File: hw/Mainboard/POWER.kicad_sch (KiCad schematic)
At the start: 67 parts, among them J10 5V PWR, J11 9V POWER, J18 PET POWER, J20 5V PWR, J7 9V POWER, U10 LM317AG-TN3-R, U13 AMS1117-3.3, U15 LM317AG-TN3-R, U17 LM317AG-TN3-R

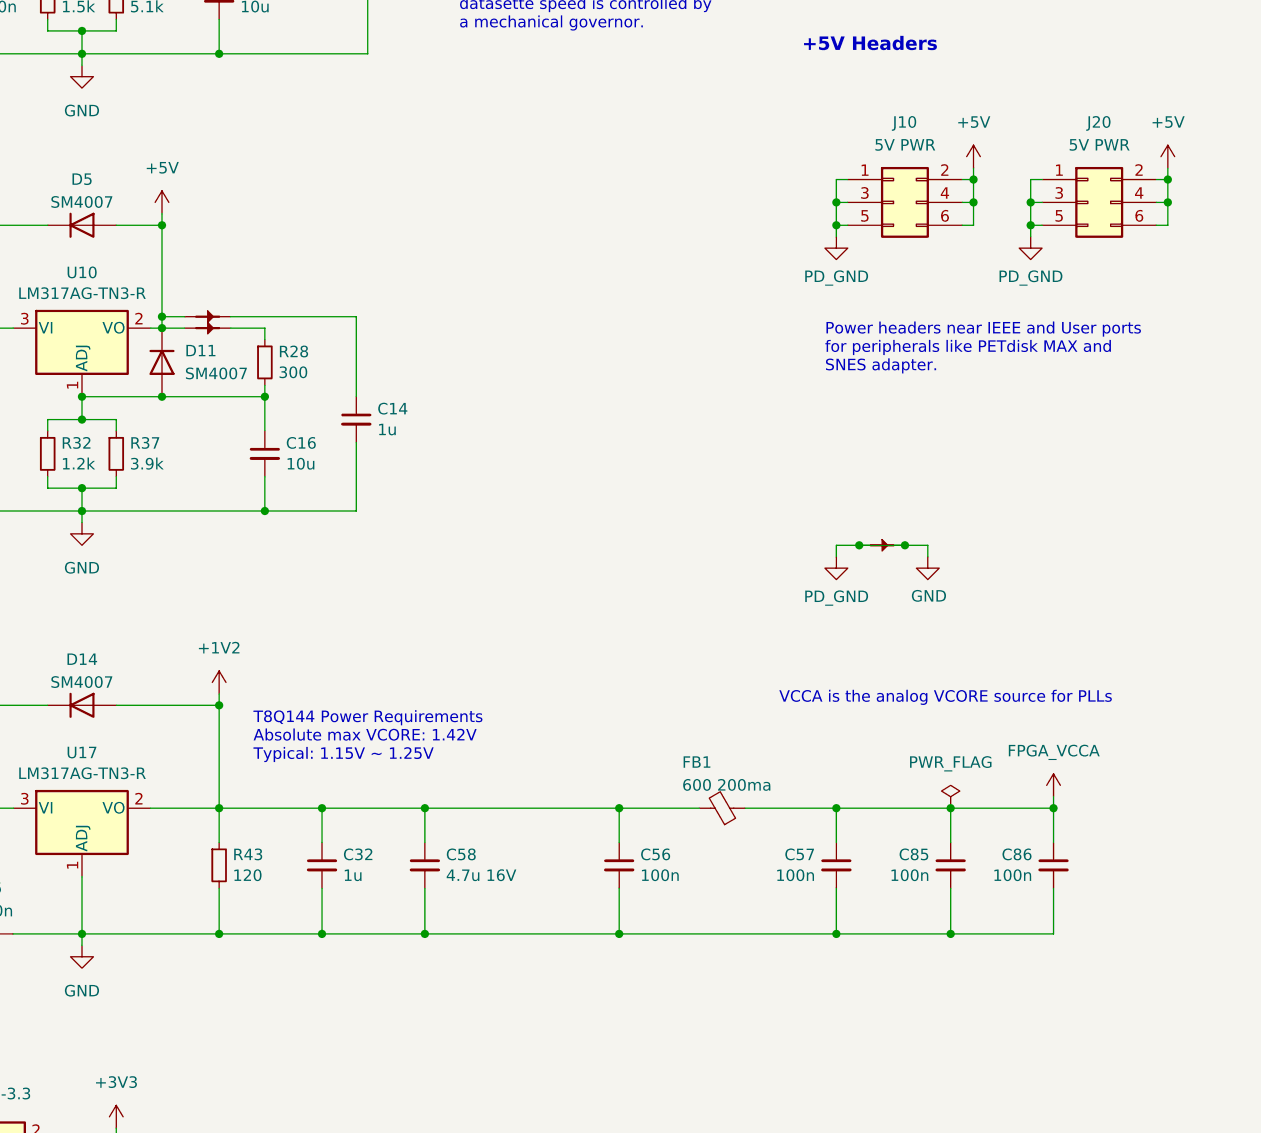
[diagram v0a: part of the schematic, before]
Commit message: hw: heat sink, trace size, more stitching
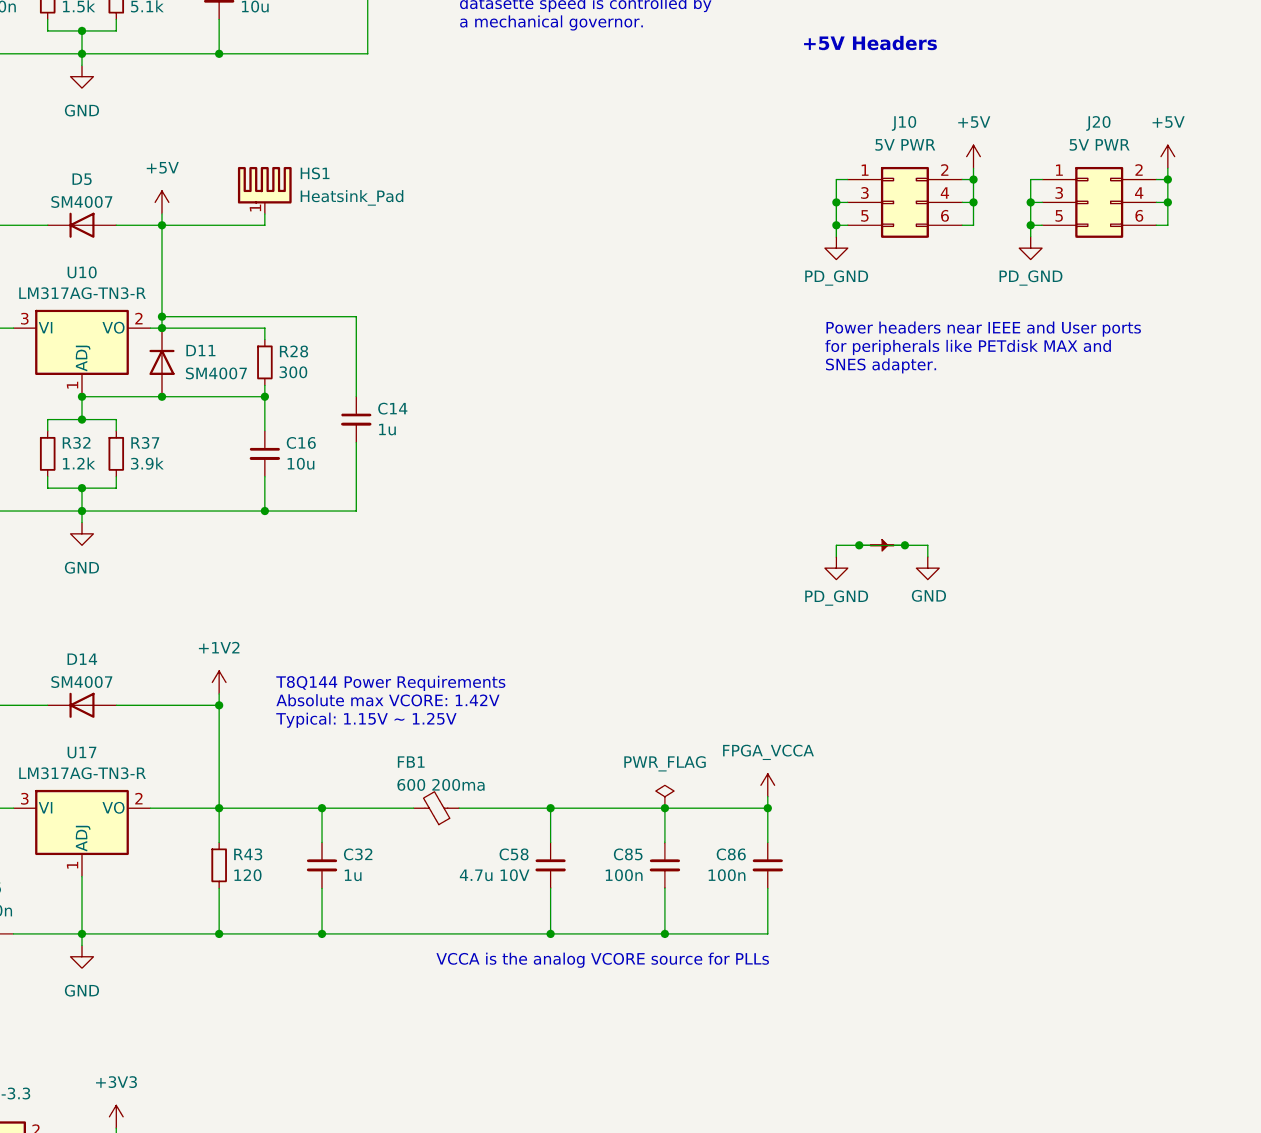
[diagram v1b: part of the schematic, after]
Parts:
- removed C56, C57: 100n, Capacitor_SMD:C_0402_1005Metric, symbol Device:C_Small
- removed PT3, PT34: PowerTie_2, PET:NetTie-2_SMD_Pad_1.6_to_0.4mm, symbol PET:PowerTie_2
- added HS1: Heatsink_Pad, PET:V1100SMDBL, symbol Mechanical:Heatsink_Pad
- C58: value 4.7u 16V -> 4.7u 10V; footprint Capacitor_SMD:C_0603_1608Metric -> Capacitor_SMD:C_0402_1005Metric; LCSC C19666 -> C23733
- U10, U15: footprint PET:TO-252-2_ThermalVias -> Package_TO_SOT_SMD:TO-252-2
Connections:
- net +1V2: no longer C58.1
- net +5V: now also C14.1, R28.1, HS1.1
- net FPGA_VCCA: now also C58.1
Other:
- moved on the sheet: C58, C85, C86, FB1

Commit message: HW: Rename 'MFR' to 'MPN' in BOM
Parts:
- HS1: MFR V-1100-SMD/B-L -> (none); MPN (none) -> V-1100-SMD/B-L
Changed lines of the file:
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@@
       (effects (font (size 1.27 1.27)) hide)
     )
-    (property "MFR" "V-1100-SMD/B-L" (id 5) (at 151.13 72.39 0)
+    (property "MPN" "V-1100-SMD/B-L" (id 6) (at 151.13 72.39 0)
       (effects (font (size 1.27 1.27)) hide)
     )

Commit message: hw: add more Mouse part numbers
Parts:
- J10, J20: MOUSER (none) -> 649-1012938195002BLF
- J11: MOUSER (none) -> 649-1012937893602BLF
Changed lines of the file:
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@@
+      (effects (font (size 1.27 1.27)) hide)
+    )
+    (property "MOUSER" "649-1012937893602BLF" (id 4) (at 87.63 41.91 0)
       (effects (font (size 1.27 1.27)) hide)
     )
@@
     )
     (property "Datasheet" "" (id 3) (at 242.57 73.66 0)
+      (effects (font (size 1.27 1.27)) hide)
+    )
+    (property "MOUSER" "649-1012938195002BLF" (id 4) (at 242.57 73.66 0)
       (effects (font (size 1.27 1.27)) hide)
     )
@@
       (effects (font (size 1.27 1.27)) hide)
     )
-    (property "Datasheet" "~" (id 3) (at 151.4348 73.66 0)
+    (property "Datasheet" "http://www.assmann-wsw.com/uploads/datasheets/ASS_0855_HS.pdf" (id 3) (at 151.4348 73.66 0)
       (effects (font (size 1.27 1.27)) hide)
     )
@@
       (effects (font (size 1.27 1.27)) hide)
     )
+    (property "MOUSER" "649-1012938195002BLF" (id 4) (at 220.98 73.66 0)
+      (effects (font (size 1.27 1.27)) hide)
+    )

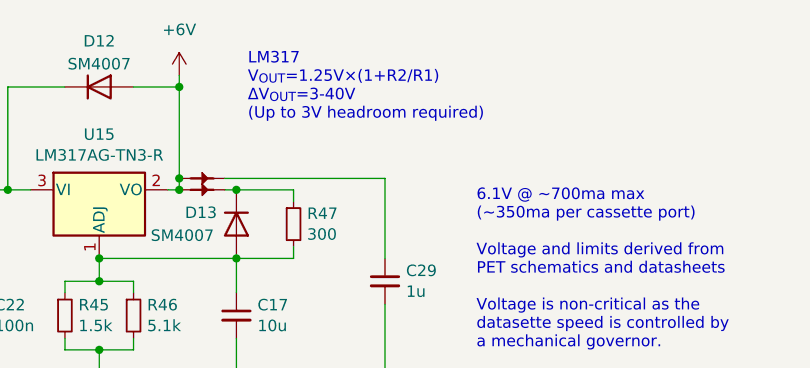
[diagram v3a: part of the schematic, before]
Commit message: hw: PN for IC, remove dup PNs, remove redundant headroom text on PWR
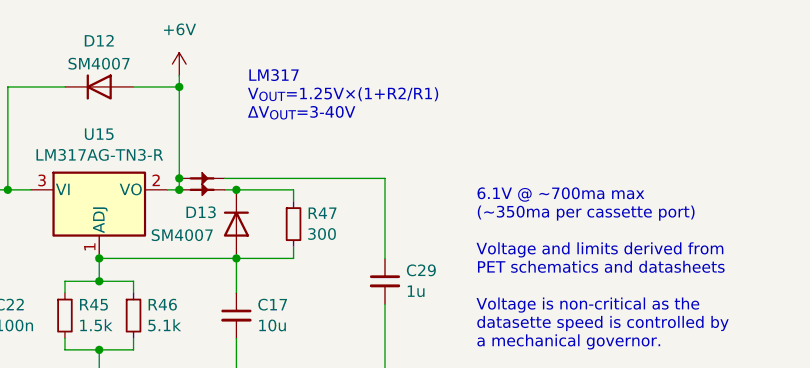
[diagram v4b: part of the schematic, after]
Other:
- note added: "LM317 V_{OUT}=1.25V×(1+R2/R1) ΔV_{OUT}=3-40V"
- note removed: "LM317 V_{OUT}=1.25V×(1+R2/R1) ΔV_{OUT}=3-40V (Up to 3V headroom required)"
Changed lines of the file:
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@@
     (effects (font (size 1.27 1.27)) (justify left bottom))
   )
-  (text "LM317\nV_{OUT}=1.25V×(1+R2/R1)\nΔV_{OUT}=3-40V\n(Up to 3V headroom required)"
-    (at 147.32 29.21 0)
+  (text "LM317\nV_{OUT}=1.25V×(1+R2/R1)\nΔV_{OUT}=3-40V" (at 147.32 29.21 0)
     (effects (font (size 1.27 1.27)) (justify left bottom))
   )

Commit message: hw: thermal vias, whitespace, refill
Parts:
- U10, U15: footprint Package_TO_SOT_SMD:TO-252-2 -> PET:TO-252-2_ThermalVias
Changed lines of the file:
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@@
     (property "Reference" "U15" (id 0) (at 130.81 30.6832 0))
     (property "Value" "LM317AG-TN3-R" (id 1) (at 130.81 32.9946 0))
-    (property "Footprint" "Package_TO_SOT_SMD:TO-252-2" (id 2) (at 130.81 30.48 0)
+    (property "Footprint" "PET:TO-252-2_ThermalVias" (id 2) (at 130.81 30.48 0)
       (effects (font (size 1.27 1.27) italic) hide)
     )
@@
     (property "Reference" "U10" (id 0) (at 130.81 81.4832 0))
     (property "Value" "LM317AG-TN3-R" (id 1) (at 130.81 83.7946 0))
-    (property "Footprint" "Package_TO_SOT_SMD:TO-252-2" (id 2) (at 130.81 81.28 0)
+    (property "Footprint" "PET:TO-252-2_ThermalVias" (id 2) (at 130.81 81.28 0)
       (effects (font (size 1.27 1.27) italic) hide)
     )

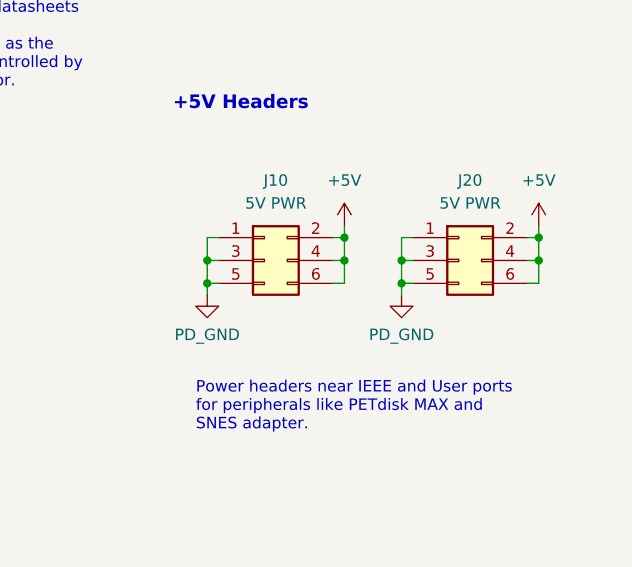
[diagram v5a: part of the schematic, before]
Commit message: hw: remove extra PWR header
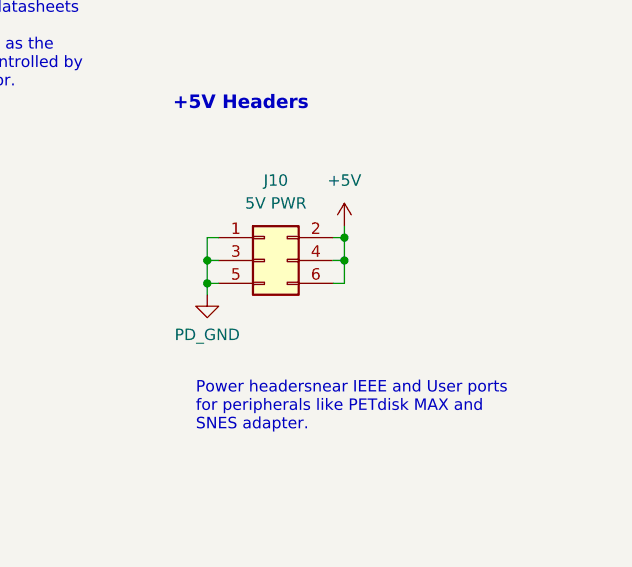
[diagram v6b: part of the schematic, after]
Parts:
- removed J20: 5V PWR, Connector_PinHeader_2.54mm:PinHeader_2x03_P2.54mm_Vertical, symbol Connector_Generic:Conn_02x03_Odd_Even
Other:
- note added: "Power headersnear IEEE and User ports for peripherals like PETdisk MAX and SNES adapter."
- note removed: "Power headers near IEEE and User ports for peripherals like PETdisk MAX and SNES adapter."
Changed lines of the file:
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@@
   (junction (at 130.81 46.99) (diameter 0) (color 0 0 0 0)
   )
-  (junction (at 236.22 76.2) (diameter 0) (color 0 0 0 0)
-  )
-  (junction (at 236.22 73.66) (diameter 0) (color 0 0 0 0)
-  )
   (junction (at 146.05 44.45) (diameter 0) (color 0 0 0 0)
   )
@@
   (junction (at 67.31 59.69) (diameter 0) (color 0 0 0 0)
   )
-  (junction (at 251.46 73.66) (diameter 0) (color 0 0 0 0)
-  )
   (junction (at 44.45 177.8) (diameter 0) (color 0 0 0 0)
   )
@@
   )
   (junction (at 139.7 87.63) (diameter 0) (color 0 0 0 0)
-  )
-  (junction (at 251.46 71.12) (diameter 0) (color 0 0 0 0)
   )
   (junction (at 157.48 140.97) (diameter 0) (color 0 0 0 0)
@@
     (stroke (width 0) (type default) (color 0 0 0 0))
   )
-  (wire (pts (xy 236.22 76.2) (xy 237.49 76.2))
-    (stroke (width 0) (type default) (color 0 0 0 0))
-  )
   (wire (pts (xy 242.57 38.1) (xy 242.57 39.37))
     (stroke (width 0) (type default) (color 0 0 0 0))
@@
     (stroke (width 0) (type default) (color 0 0 0 0))
   )
-  (wire (pts (xy 236.22 76.2) (xy 236.22 77.47))
-    (stroke (width 0) (type default) (color 0 0 0 0))
-  )
   (wire (pts (xy 130.81 46.99) (xy 127 46.99))
     (stroke (width 0) (type default) (color 0 0 0 0))
@@
     (stroke (width 0) (type default) (color 0 0 0 0))
   )
-  (wire (pts (xy 250.19 71.12) (xy 251.46 71.12))
-    (stroke (width 0) (type default) (color 0 0 0 0))
-  )
   (wire (pts (xy 116.84 36.83) (xy 116.84 38.1))
     (stroke (width 0) (type default) (color 0 0 0 0))
@@
     (stroke (width 0) (type default) (color 0 0 0 0))
   )
-  (wire (pts (xy 236.22 71.12) (xy 237.49 71.12))
-    (stroke (width 0) (type default) (color 0 0 0 0))
-  )
   (wire (pts (xy 182.88 140.97) (xy 172.72 140.97))
     (stroke (width 0) (type default) (color 0 0 0 0))
@@
     (stroke (width 0) (type default) (color 0 0 0 0))
   )
-  (wire (pts (xy 251.46 69.85) (xy 251.46 71.12))
-    (stroke (width 0) (type default) (color 0 0 0 0))
-  )
   (wire (pts (xy 228.6 76.2) (xy 229.87 76.2))
     (stroke (width 0) (type default) (color 0 0 0 0))
@@
     (stroke (width 0) (type default) (color 0 0 0 0))
   )
-  (wire (pts (xy 251.46 71.12) (xy 251.46 73.66))
-    (stroke (width 0) (type default) (color 0 0 0 0))
-  )
   (wire (pts (xy 139.7 86.36) (xy 161.29 86.36))
     (stroke (width 0) (type default) (color 0 0 0 0))
@@
     (stroke (width 0) (type default) (color 0 0 0 0))
   )
-  (wire (pts (xy 251.46 73.66) (xy 251.46 76.2))
-    (stroke (width 0) (type default) (color 0 0 0 0))
-  )
   (wire (pts (xy 214.63 111.76) (xy 217.17 111.76))
     (stroke (width 0) (type default) (color 0 0 0 0))
@@
     (stroke (width 0) (type default) (color 0 0 0 0))
   )
-  (wire (pts (xy 250.19 76.2) (xy 251.46 76.2))
-    (stroke (width 0) (type default) (color 0 0 0 0))
-  )
   (wire (pts (xy 76.2 74.93) (xy 80.01 74.93))
     (stroke (width 0) (type default) (color 0 0 0 0))
@@
     (stroke (width 0) (type default) (color 0 0 0 0))
   )
-  (wire (pts (xy 236.22 73.66) (xy 237.49 73.66))
-    (stroke (width 0) (type default) (color 0 0 0 0))
-  )
   (wire (pts (xy 151.13 76.2) (xy 151.13 74.93))
     (stroke (width 0) (type default) (color 0 0 0 0))
@@
     (stroke (width 0) (type default) (color 0 0 0 0))
   )
-  (wire (pts (xy 236.22 73.66) (xy 236.22 76.2))
-    (stroke (width 0) (type default) (color 0 0 0 0))
-  )
   (wire (pts (xy 64.77 36.83) (xy 82.55 36.83))
     (stroke (width 0) (type default) (color 0 0 0 0))
@@
     (stroke (width 0) (type default) (color 0 0 0 0))
   )
-  (wire (pts (xy 250.19 73.66) (xy 251.46 73.66))
-    (stroke (width 0) (type default) (color 0 0 0 0))
-  )
   (wire (pts (xy 49.53 36.83) (xy 49.53 64.77))
     (stroke (width 0) (type default) (color 0 0 0 0))
   )
   (wire (pts (xy 130.81 154.94) (xy 130.81 156.21))
-    (stroke (width 0) (type default) (color 0 0 0 0))
-  )
-  (wire (pts (xy 236.22 71.12) (xy 236.22 73.66))
     (stroke (width 0) (type default) (color 0 0 0 0))
   )
@@
     (effects (font (size 1.5 1.5) (thickness 0.8) bold) (justify left bottom))
   )
-  (text "Power headers near IEEE and User ports\nfor peripherals like PETdisk MAX and\nSNES adapter."
+  (text "Power headersnear IEEE and User ports\nfor peripherals like PETdisk MAX and\nSNES adapter."
     (at 213.36 92.71 0)
     (effects (font (size 1.27 1.27)) (justify left bottom))
@@
     (pin "1")
   )
-  (symbol (lib_id "PET:PD_GND") (at 236.22 77.47 0) (unit 1)
-    (in_bom yes) (on_board yes)
-    (property "Reference" "#PWR0183" (id 0) (at 236.22 83.82 0)
-      (effects (font (size 1.27 1.27)) hide)
-    )
-    (property "Value" "PD_GND" (id 1) (at 236.22 81.915 0))
-    (property "Footprint" "" (id 2) (at 236.22 77.47 0)
-      (effects (font (size 1.27 1.27)) hide)
-    )
-    (property "Datasheet" "" (id 3) (at 236.22 77.47 0)
-      (effects (font (size 1.27 1.27)) hide)
-    )
-    (pin "1")
-  )
   (symbol (lib_id "Connector:Conn_01x02_Male") (at 87.63 41.91 180) (unit 1)
     (in_bom yes) (on_board yes) (fields_autoplaced)
@@
     )
     (property "Datasheet" "" (id 3) (at 40.64 44.45 0)
-      (effects (font (size 1.27 1.27)) hide)
-    )
-    (pin "1")
-  )
-  (symbol (lib_id "power:+5V") (at 251.46 69.85 0) (unit 1)
-    (in_bom yes) (on_board yes) (fields_autoplaced)
-    (property "Reference" "#PWR0195" (id 0) (at 251.46 73.66 0)
-      (effects (font (size 1.27 1.27)) hide)
-    )
-    (property "Value" "+5V" (id 1) (at 251.46 64.77 0))
-    (property "Footprint" "" (id 2) (at 251.46 69.85 0)
-      (effects (font (size 1.27 1.27)) hide)
-    )
-    (property "Datasheet" "" (id 3) (at 251.46 69.85 0)
       (effects (font (size 1.27 1.27)) hide)
     )
@@
     (pin "2")
   )
-  (symbol (lib_id "Connector_Generic:Conn_02x03_Odd_Even") (at 242.57 73.66 0) (unit 1)
-    (in_bom yes) (on_board yes) (fields_autoplaced)
-    (property "Reference" "J20" (id 0) (at 243.84 64.77 0))
-    (property "Value" "5V PWR" (id 1) (at 243.84 67.31 0))
-    (property "Footprint" "Connector_PinHeader_2.54mm:PinHeader_2x03_P2.54mm_Vertical" (id 2) (at 242.57 73.66 0)
-      (effects (font (size 1.27 1.27)) hide)
-    )
-    (property "Datasheet" "" (id 3) (at 242.57 73.66 0)
-      (effects (font (size 1.27 1.27)) hide)
-    )
-    (property "MOUSER" "649-1012938195002BLF" (id 4) (at 242.57 73.66 0)
-      (effects (font (size 1.27 1.27)) hide)
-    )
-    (pin "1")
-    (pin "2")
-    (pin "3")
-    (pin "4")
-    (pin "5")
-    (pin "6")
-  )
   (symbol (lib_id "power:GND") (at 130.81 156.21 0) (unit 1)
